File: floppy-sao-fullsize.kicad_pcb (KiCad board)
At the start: 2 copper layers, 85.6 x 89.9 mm, 13 parts, among them Q1 2N7002, U1 M24C02-WMN, U2 M24C02-WMN, X1 Badgelife_sao_connector_v169b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

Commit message: feat: add order number placeholder
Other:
- board text added: "JLCJLCJLCJLC"
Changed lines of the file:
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@@
   (general
     (thickness 1.6)
-    (drawings 17)
+    (drawings 18)
     (tracks 110)
     (zones 0)
@@
     (visible_elements 7FFFFFFF)
     (pcbplotparams
-      (layerselection 0x010f0_80000001)
+      (layerselection 0x010f0_ffffffff)
       (usegerberextensions false)
       (usegerberattributes false)
@@
       (outputformat 1)
       (mirror false)
-      (drillshape 1)
+      (drillshape 0)
       (scaleselection 1)
-      (outputdirectory "gerbers/"))
+      (outputdirectory "gerber/fullsize"))
   )
   (net 0 "")
@@
     )
   )
+  (gr_text JLCJLCJLCJLC (at 146.8 114.75) (layer B.SilkS)
+    (effects (font (size 0.8 0.8) (thickness 0.15)) (justify mirror))
+  )
   (gr_text "© 2019, Uri Shaked" (at 150.5 117.8) (layer B.SilkS)

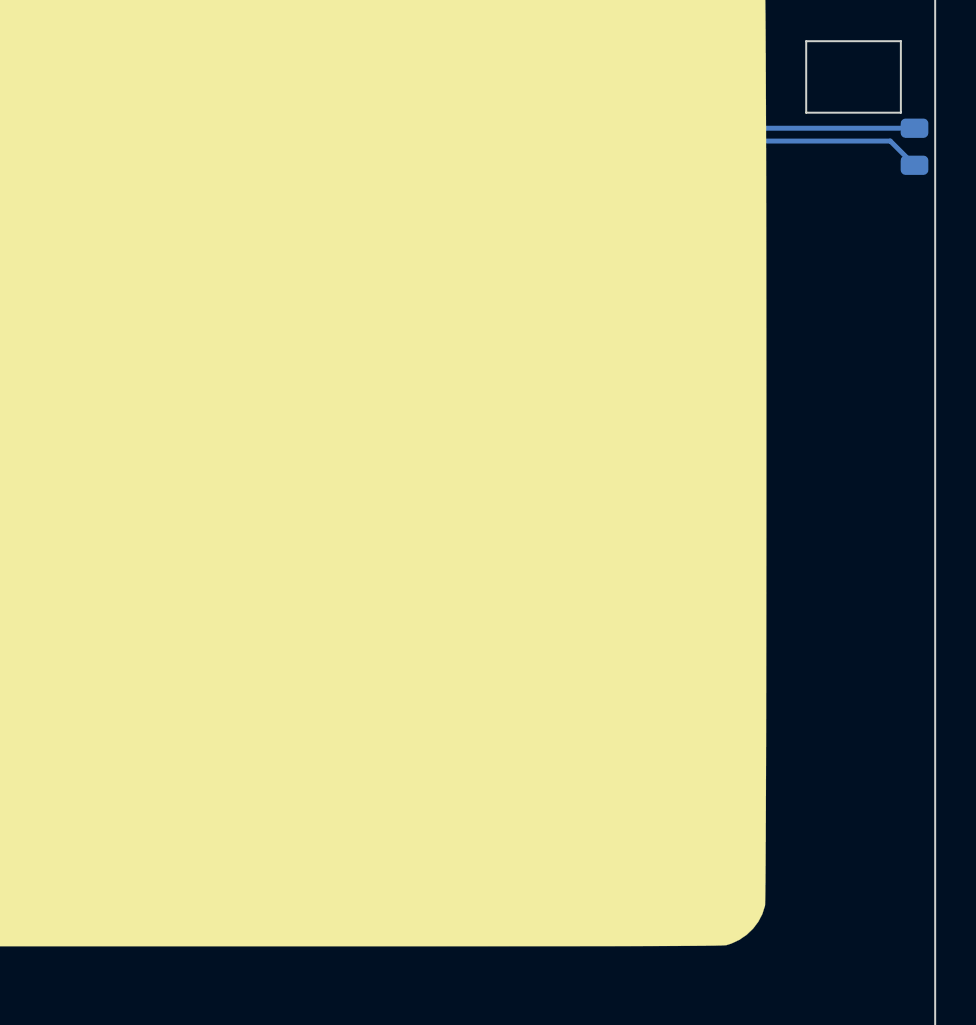
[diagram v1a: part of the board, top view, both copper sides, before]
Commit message: fix: activity LED logic inverted
It should be on when SCL is low and not high
Replaced N-Channel MOSFET with a P-Channel MOSFET.
Also enlarged LED silk screen drawing.
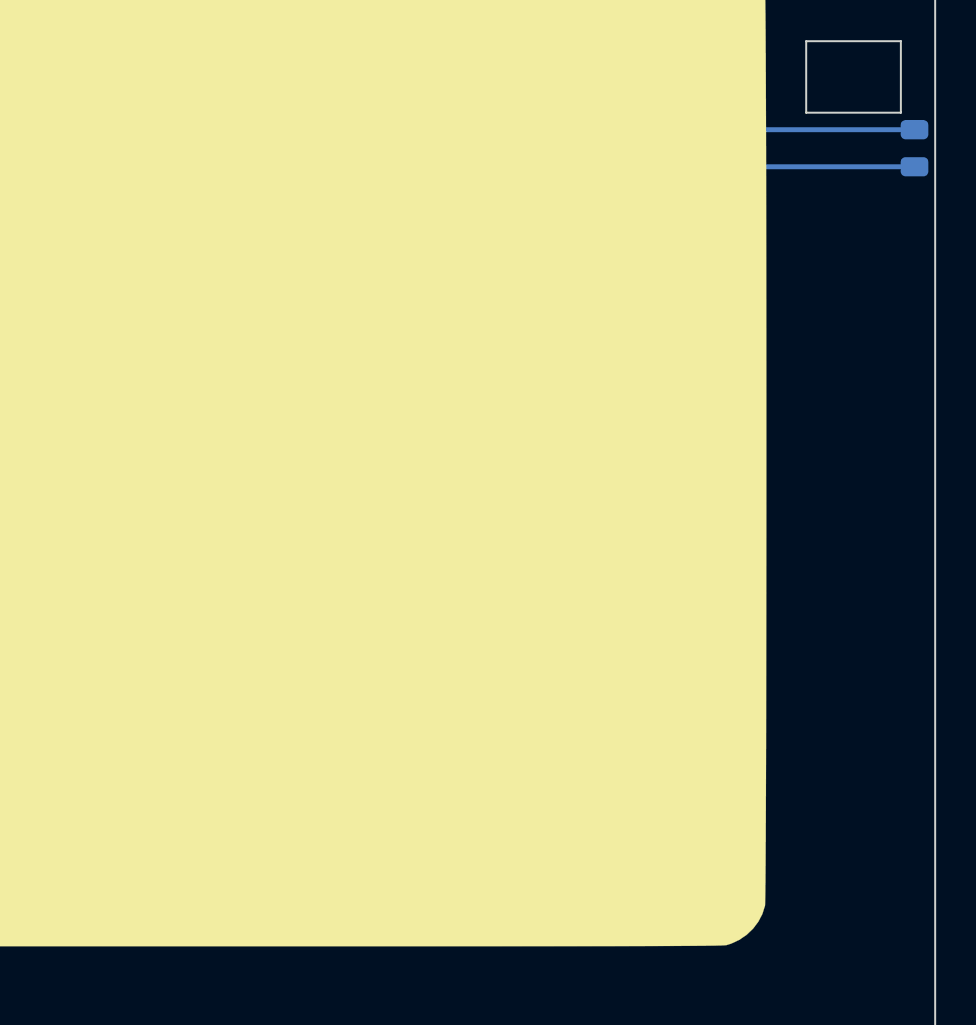
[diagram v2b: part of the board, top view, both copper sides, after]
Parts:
- Q1: value 2N7002 -> TP0610T
- U2: value M24C02-WMN -> AT24C256C
- moved Q1 0.90 mm to (160.8, 108.2)
- moved D1 0.08 mm to (191.8, 72.0), turned to 270 degrees
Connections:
- D1 pad 2: VCC -> Net-(D1-Pad2)
- Q1 pad 2: GND -> VCC
- Q1 pad 3: Net-(Q1-Pad3) -> Net-(D1-Pad2)
- R1 pad 1: Net-(Q1-Pad3) -> GND
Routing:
- net Net-(D1-Pad2): track 0.00 -> 56.4 mm
- net VCC: track 103.3 -> 72.3 mm
- net GND: track 66.6 -> 71.5 mm
- net Net-(Q1-Pad3): track 4.55 -> 0.00 mm
- net /SCL: track 30.2 -> 31.4 mm

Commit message: feat: replace conference logo with Wokwi logo
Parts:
- added logo1: Val**, floppy:wokwi-large, B.Cu at (114.6, 103.0)
